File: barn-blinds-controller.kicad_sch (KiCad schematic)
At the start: 20 parts, among them J1 Power Input, J2 Motor 1 Output, J3 Motor 2 Output, J4 Motor 3 Output, M1 Blind 1, M2 Blind 2, M3 Blind 3, U1 ESP32-DevKitC, U2 TB6612, U3 TB6612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

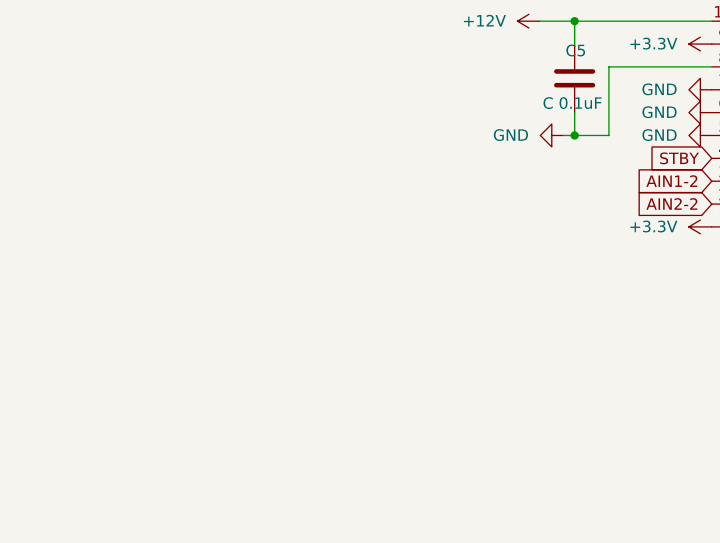
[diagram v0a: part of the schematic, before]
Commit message: Added hierarchical sheets for custom pcb design
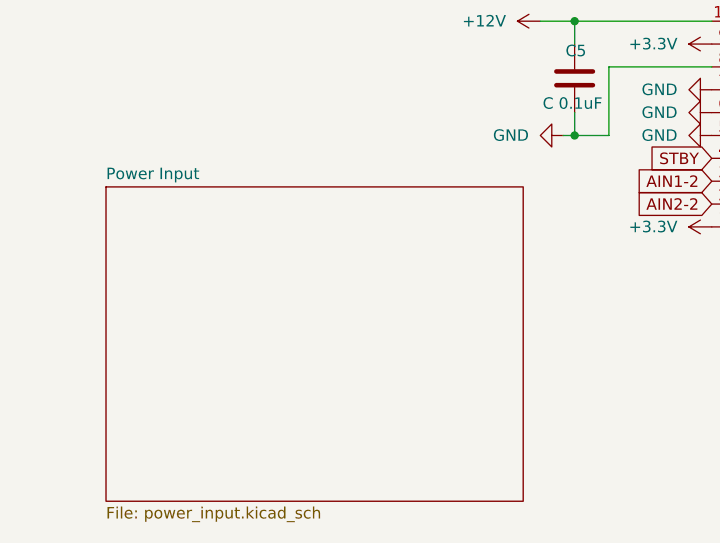
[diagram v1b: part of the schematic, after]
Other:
- added sheet Power Input (power_input.kicad_sch)
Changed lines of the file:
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@@
+		)
+	)
+	(sheet
+		(at 24.13 146.685)
+		(size 46.355 34.925)
+		(exclude_from_sim no)
+		(in_bom yes)
+		(on_board yes)
+		(dnp no)
+		(fields_autoplaced yes)
+		(stroke
+			(width 0.1524)
+			(type solid)
+		)
+		(fill
+			(color 0 0 0 0.0000)
+		)
+		(property "Sheetname" "Power Input"
+			(at 24.13 145.9734 0)
+			(effects
+				(font
+					(size 1.27 1.27)
+				)
+				(justify left bottom)
+			)
+		)
+		(property "Sheetfile" "power_input.kicad_sch"
+			(at 24.13 182.1946 0)
+			(effects
+				(font
+					(size 1.27 1.27)
+				)
+				(justify left top)
+			)
+		)
+		(instances
+			(project "barn-blinds-controller"
+				(path "/aa90962a-81b9-423d-8acd-c4e83fa798bb"
+					(page "2")
+				)
+			)
 		)
 	)

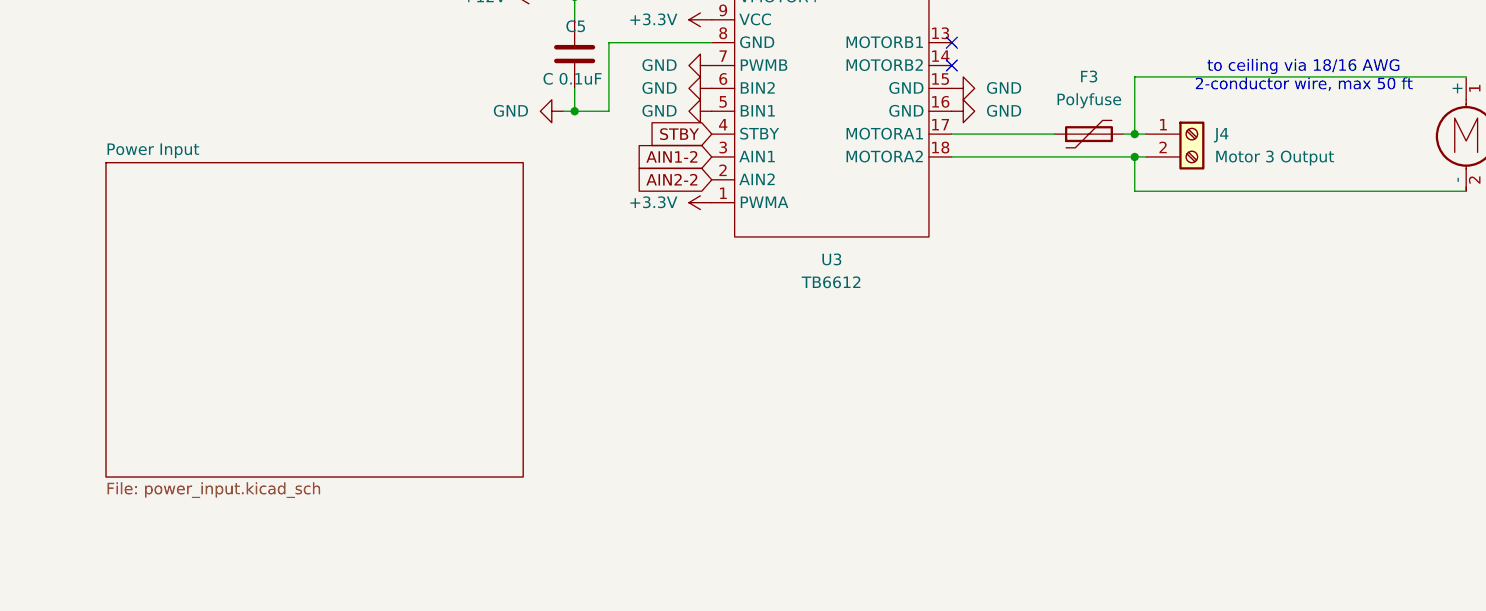
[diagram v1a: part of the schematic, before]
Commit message: adding hierachical sheets: Isolated circuits, esp32, etc
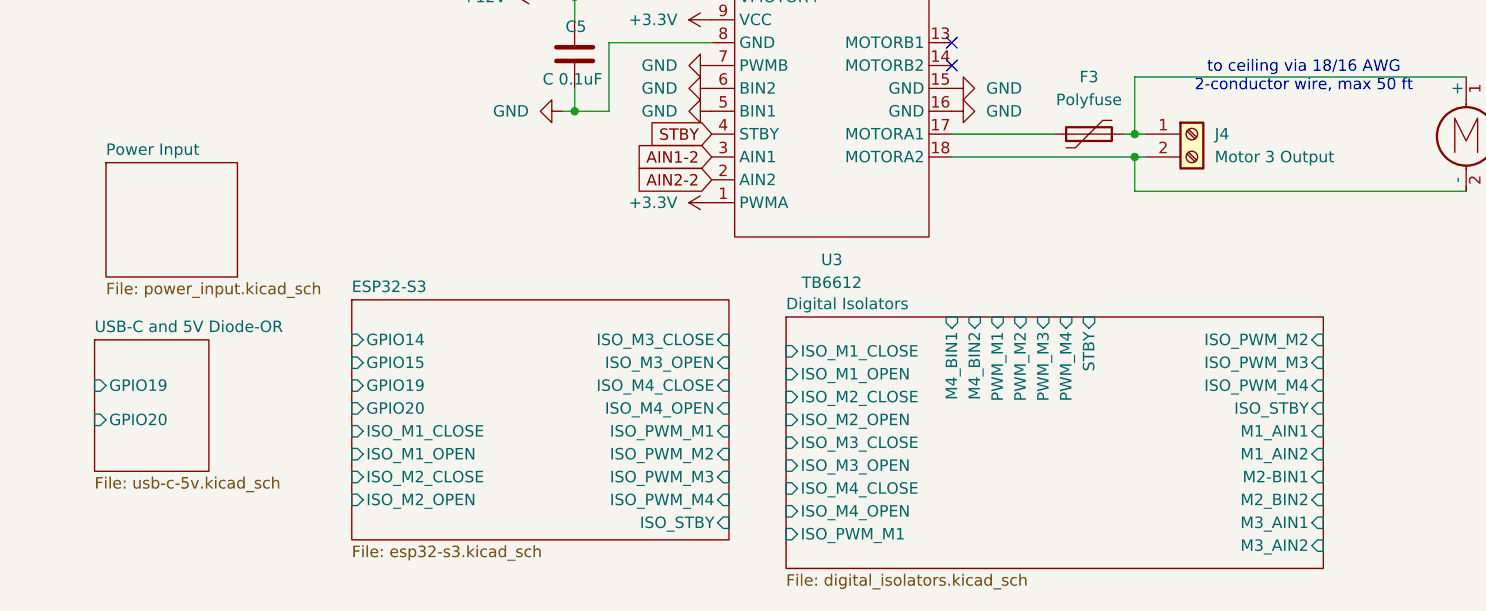
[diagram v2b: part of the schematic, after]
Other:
- added sheet Digital Isolators (digital_isolators.kicad_sch)
- added sheet ESP32-S3 (esp32-s3.kicad_sch)
- added sheet USB-C and 5V Diode-OR (usb-c-5v.kicad_sch)

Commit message: Started running traces
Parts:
- removed C1, C2: 2200uF 25V Polarized, symbol Device:C_Polarized
- removed C3: 1000uF 10V, symbol Device:C_Polarized
- removed C4, C5: C 0.1uF, symbol Device:C
- removed F1, F2, F3: Polyfuse, symbol Device:Polyfuse
- removed J1: Power Input, symbol Connector:Screw_Terminal_01x02
- removed J2: Motor 1 Output, symbol Connector:Screw_Terminal_01x02
- removed J3: Motor 2 Output, symbol Connector:Screw_Terminal_01x02
- removed J4: Motor 3 Output, symbol Connector:Screw_Terminal_01x02
- removed M1: Blind 1, symbol Motor:Motor_DC
- removed M2: Blind 2, symbol Motor:Motor_DC
- removed M3: Blind 3, symbol Motor:Motor_DC
- removed R1: R 10K, symbol Device:R
- removed U1: ESP32-DevKitC, PCM_Espressif:ESP32-DevKitC, symbol PCM_Espressif:ESP32-DevKitC
- removed U2, U3: TB6612, symbol New_Library:TB6612_Breakout
- removed U4: LM2596 Buck Converter 12-5, Package_TO_SOT_SMD:TO-263-5_TabPin3, symbol Regulator_Switching:LM2596S-3.3
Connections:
- no-connect marks 34 -> 0
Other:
- added sheet Motor Drivers and Power (motor_drivers.kicad_sch)
- added sheet Motor Outputs (motor_outputs.kicad_sch)
- added sheet Sensors (sensors.kicad_sch)
- sheet Digital Isolators ports: added M2_BIN1; removed M2-BIN1
- note removed: "to ceiling via 18/16 AWG 2-conductor wire, max 50 ft"

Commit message: PCB tracing complete
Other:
- sheet Motor Drivers and Power ports: added none; removed U2_A01, U2_A02, U2_B01, U2_B02, U3_A01, U3_A02, U3_B01, U3_B02
- sheet Motor Outputs ports: added none; removed U2_A01, U2_A02, U2_B01, U2_B02, U3_A01, U3_A02, U3_B01, U3_B02

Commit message: Reworking with new terminal block, adding mounting holes.  Need to rerun a number of traces.
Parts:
- added H1, H2, H3, H4: MountingHole, MountingHole:MountingHole_2.2mm_M2, symbol Mechanical:MountingHole

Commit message: BOM work
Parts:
- renumbered H2 to H1, H1 to H2, H4 to H3, H3 to H4
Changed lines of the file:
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@@
 		(dnp no)
 		(fields_autoplaced yes)
-		(property "Reference" "H4"
+		(property "Reference" "H3"
 			(at 275.59 153.6699 0)
 			(effects
@@
 			(project "barn-blinds-controller"
 				(path "/aa90962a-81b9-423d-8acd-c4e83fa798bb"
-					(reference "H4")
+					(reference "H3")
 					(unit 1)
 				)
@@
 		(dnp no)
 		(fields_autoplaced yes)
-		(property "Reference" "H2"
+		(property "Reference" "H1"
 			(at 20.32 16.5099 0)
 			(effects
@@
 			(project "barn-blinds-controller"
 				(path "/aa90962a-81b9-423d-8acd-c4e83fa798bb"
-					(reference "H2")
+					(reference "H1")
 					(unit 1)
 				)
@@
 		(dnp no)
 		(fields_autoplaced yes)
-		(property "Reference" "H3"
+		(property "Reference" "H4"
 			(at 276.86 19.0499 0)
 			(effects
@@
 			(project "barn-blinds-controller"
 				(path "/aa90962a-81b9-423d-8acd-c4e83fa798bb"
-					(reference "H3")
+					(reference "H4")
 					(unit 1)
 				)
@@
 		(dnp no)
 		(fields_autoplaced yes)
-		(property "Reference" "H1"
+		(property "Reference" "H2"
 			(at 26.67 184.1499 0)
 			(effects
@@
 			(project "barn-blinds-controller"
 				(path "/aa90962a-81b9-423d-8acd-c4e83fa798bb"
-					(reference "H1")
-					(unit 1)
-				)
+					(reference "H2")
+					(unit 1)
+				)

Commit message: Final cleanup
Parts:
- H1, H2, H3, H4: footprint MountingHole:MountingHole_2.2mm_M2 -> MountingHole:MountingHole_3.2mm_M3
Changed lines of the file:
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@@
 			)
 		)
-		(property "Footprint" "MountingHole:MountingHole_2.2mm_M2"
+		(property "Footprint" "MountingHole:MountingHole_3.2mm_M3"
 			(at 273.05 154.94 0)
 			(effects
@@
 			)
 		)
-		(property "Footprint" "MountingHole:MountingHole_2.2mm_M2"
+		(property "Footprint" "MountingHole:MountingHole_3.2mm_M3"
 			(at 17.78 17.78 0)
 			(effects
@@
 			)
 		)
-		(property "Footprint" "MountingHole:MountingHole_2.2mm_M2"
+		(property "Footprint" "MountingHole:MountingHole_3.2mm_M3"
 			(at 274.32 20.32 0)
 			(effects
@@
 			)
 		)
-		(property "Footprint" "MountingHole:MountingHole_2.2mm_M2"
+		(property "Footprint" "MountingHole:MountingHole_3.2mm_M3"
 			(at 24.13 185.42 0)
 			(effects

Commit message: V 1.2
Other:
- sheet ESP32-S3 ports: added ACS723, TMP235, USB_DN, USB_DP; removed GPIO14, GPIO15, GPIO19, GPIO20
- sheet Sensors ports: added ACS723, TMP235; removed GPIO14, GPIO15
- sheet USB-C and 5V Diode-OR ports: added USB_DN, USB_DP; removed GPIO19, GPIO20
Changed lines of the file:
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@@
 		)
 	)
-	(label "GPIO20"
+	(label "USB_DP"
 		(at 34.29 63.5 180)
 		(effects
@@
 		)
 	)
-	(label "GPIO14"
+	(label "ACS723"
 		(at 34.29 99.06 180)
 		(effects
@@
 		)
 	)
-	(label "GPIO15"
+	(label "TMP235"
 		(at 34.29 102.87 180)
 		(effects
@@
 		)
 	)
-	(label "GPIO19"
+	(label "USB_DN"
 		(at 34.29 59.69 180)
 		(effects
@@
 		)
 	)
-	(label "GPIO20"
+	(label "USB_DP"
 		(at 91.44 35.56 180)
 		(effects
@@
 		)
 	)
-	(label "GPIO15"
+	(label "TMP235"
 		(at 91.44 30.48 180)
 		(effects
@@
 		)
 	)
-	(label "GPIO19"
+	(label "USB_DN"
 		(at 91.44 33.02 180)
 		(effects
@@
 		)
 	)
-	(label "GPIO14"
+	(label "ACS723"
 		(at 91.44 27.94 180)
 		(effects
@@
 			)
 		)
-		(pin "GPIO14" input
-			(at 91.44 27.94 180)
-			(effects
-				(font
-					(size 1.27 1.27)
-				)
-				(justify left)
-			)
-		)
-		(pin "GPIO15" input
-			(at 91.44 30.48 180)
-			(effects
-				(font
-					(size 1.27 1.27)
-				)
-				(justify left)
-			)
-		)
-		(pin "GPIO19" input
-			(at 91.44 33.02 180)
-			(effects
-				(font
-					(size 1.27 1.27)
-				)
-				(justify left)
-			)
-		)
-		(pin "GPIO20" input
-			(at 91.44 35.56 180)
-			(effects
-				(font
-					(size 1.27 1.27)
-				)
-				(justify left)
-			)
-		)
 		(pin "ISO_M1_CLOSE" input
 			(at 91.44 38.1 180)
@@
 				)
 				(justify right)
+			)
+		)
+		(pin "USB_DN" input
+			(at 91.44 33.02 180)
+			(effects
+				(font
+					(size 1.27 1.27)
+				)
+				(justify left)
+			)
+		)
+		(pin "USB_DP" input
+			(at 91.44 35.56 180)
+			(effects
+				(font
+					(size 1.27 1.27)
+				)
+				(justify left)
+			)
+		)
+		(pin "ACS723" input
+			(at 91.44 27.94 180)
+			(effects
+				(font
+					(size 1.27 1.27)
+				)
+				(justify left)
+			)
+		)
+		(pin "TMP235" input
+			(at 91.44 30.48 180)
+			(effects
+				(font
+					(size 1.27 1.27)
+				)
+				(justify left)
 			)
 		)
@@
 			)
 		)
-		(pin "GPIO19" input
+		(pin "USB_DN" input
 			(at 34.29 59.69 180)
 			(effects
@@
 			)
 		)
-		(pin "GPIO20" input
+		(pin "USB_DP" input
 			(at 34.29 63.5 180)
 			(effects
@@
 	(sheet
 		(at 91.44 68.58)
-		(size 44.45 44.45)
+		(size 44.45 40.005)
 		(exclude_from_sim no)
 		(in_bom yes)
@@
 		)
 		(property "Sheetfile" "digital_isolators.kicad_sch"
-			(at 91.44 113.6146 0)
+			(at 91.44 109.1696 0)
 			(effects
 				(font
@@
 			)
 		)
-		(pin "GPIO14" input
+		(pin "ACS723" input
 			(at 34.29 99.06 180)
 			(effects
@@
 			)
 		)
-		(pin "GPIO15" input
+		(pin "TMP235" input
 			(at 34.29 102.87 180)
 			(effects
